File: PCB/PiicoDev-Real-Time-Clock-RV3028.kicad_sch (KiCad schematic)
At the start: 26 parts

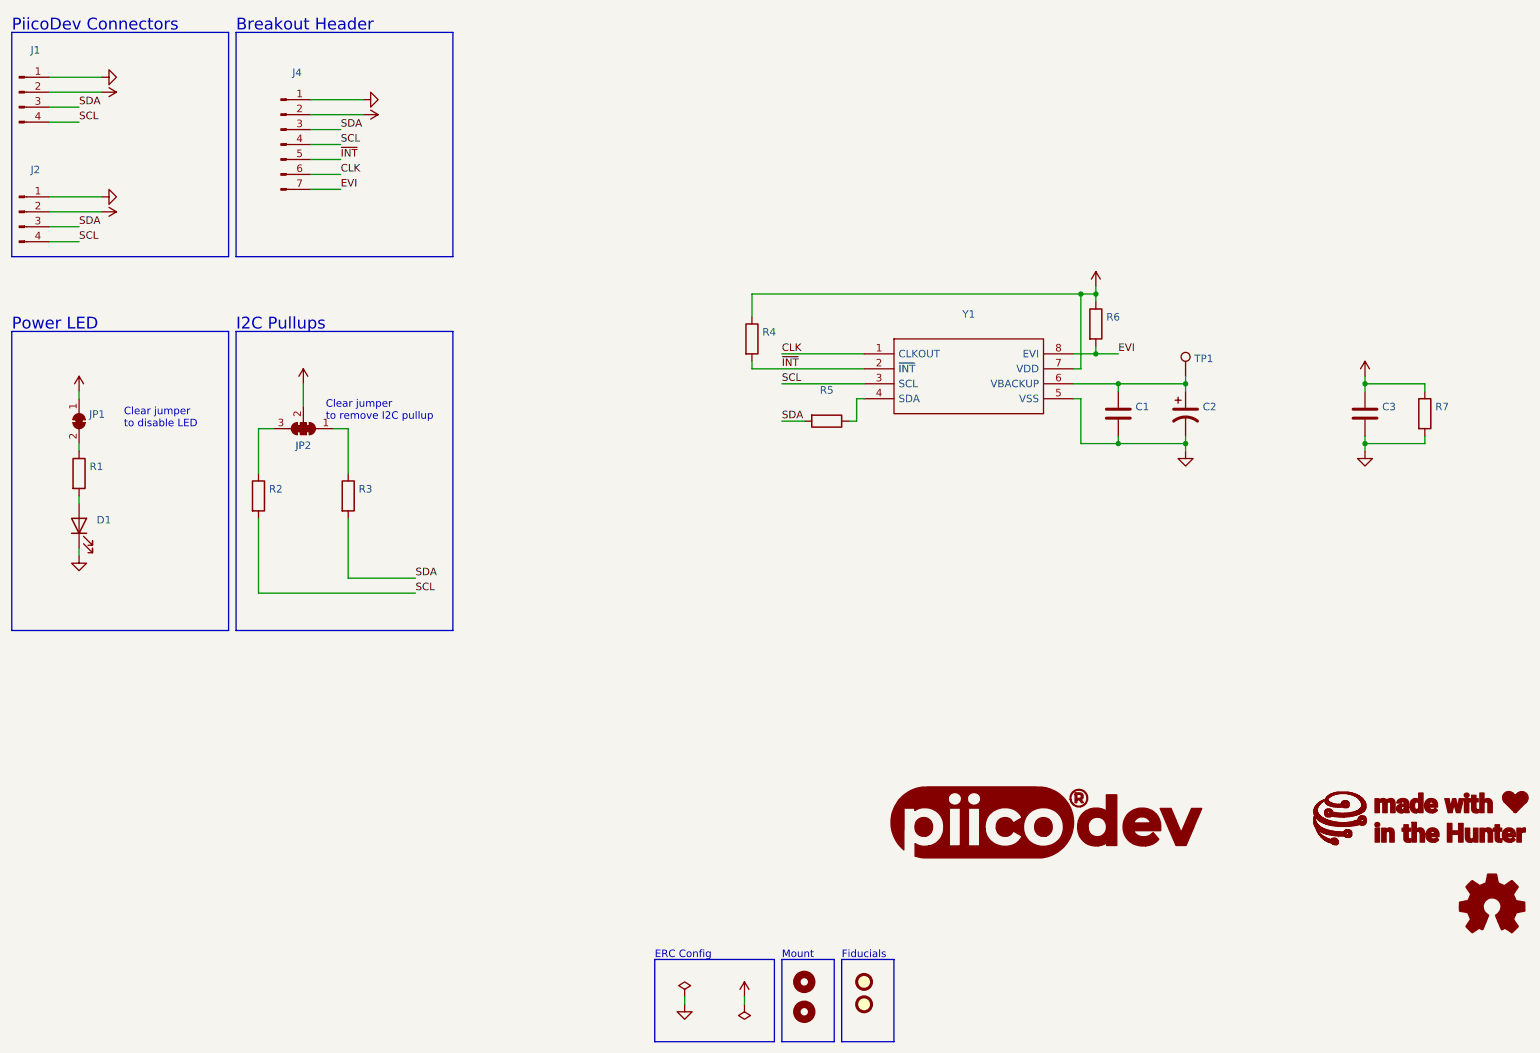
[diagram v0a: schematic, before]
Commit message: complete updgrade to KiCad v6, clean up repo
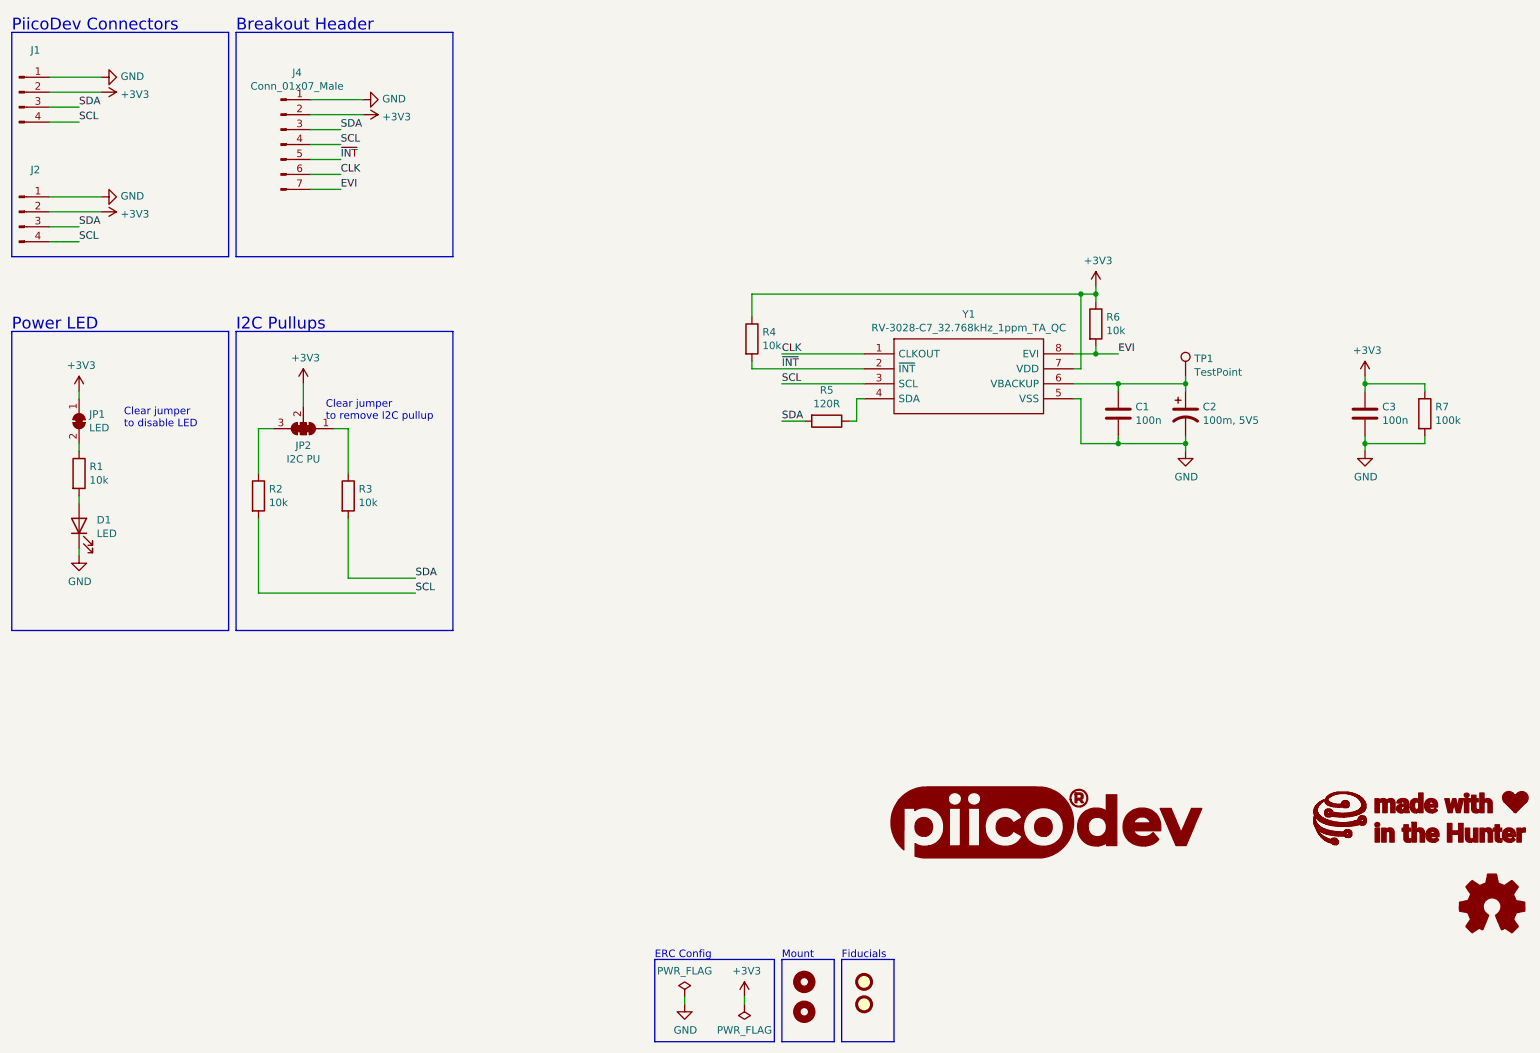
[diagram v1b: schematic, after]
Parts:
- C1, C3: value (none) -> 100n; footprint (none) -> Capacitor_SMD:C_0402_1005Metric
- C2: value (none) -> 100m, 5V5; footprint (none) -> CoreElectronics_Components:Kemet_FC_10.5X5.5
- D1: value (none) -> LED; footprint (none) -> LED_SMD:LED_0603_1608Metric
- FID1, FID2: value (none) -> Fiducial; footprint (none) -> Fiducial:Fiducial_1mm_Mask2mm
- G1: value (none) -> LOGO_PiicoDev; footprint (none) -> CoreElectronics_Artwork:piicodev_logo_14.2x3.4mm
- G2: value (none) -> LOGO_CoreElectronics_no-text; footprint (none) -> CoreElectronics_Artwork:CoreElectronics_logo_5mm
- G3: value (none) -> LOGO_made-with-love; footprint (none) -> CoreElectronics_Artwork:piicodev_logo_14.2x3.4mm
- H1, H2: value (none) -> MountingHole; footprint (none) -> CoreElectronics_Components:MountingHole_2.7mm_M2.5_PadClearance_1.2
- J1, J2: value (none) -> (none); footprint (none) -> Connector_JST:JST_SH_SM04B-SRSS-TB_1x04-1MP_P1.00mm_Horizontal
- J4: value (none) -> Conn_01x07_Male; footprint (none) -> PiicoDev Real Time Clock RV3028:PinHeader_1x07_P2.54mm_Vertical
- JP1: value (none) -> LED; footprint (none) -> CoreElectronics_Components:SolderJumper-2_P1.3mm_Bridged_RoundedPad1.0x1.5mm
- JP2: value (none) -> I2C PU; footprint (none) -> CoreElectronics_Components:SolderJumper-3_P1.3mm_Closed_RoundedPad1.0x1.5mm_NumberLabels
- LOGO1: value (none) -> Logo_Open_Hardware_Small; footprint (none) -> CoreElectronics_Artwork:oshw
- R1, R2, R3, R4, R6: value (none) -> 10k; footprint (none) -> Resistor_SMD:R_0402_1005Metric
- R5: value (none) -> 120R; footprint (none) -> Resistor_SMD:R_0402_1005Metric
- R7: value (none) -> 100k; footprint (none) -> Resistor_SMD:R_0402_1005Metric
- TP1: value (none) -> TestPoint; footprint (none) -> PiicoDev Real Time Clock RV3028:PinHeader_1x01_P2.54mm_Vertical
- Y1: value (none) -> RV-3028-C7_32.768kHz_1ppm_TA_QC; footprint (none) -> CoreElectronics_Components:MicroCrystal_RV3028C7
